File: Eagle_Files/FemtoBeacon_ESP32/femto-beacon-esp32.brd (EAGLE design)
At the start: 59.4 x 82.5 mm, 64 parts, among them IC1 FT232RQ

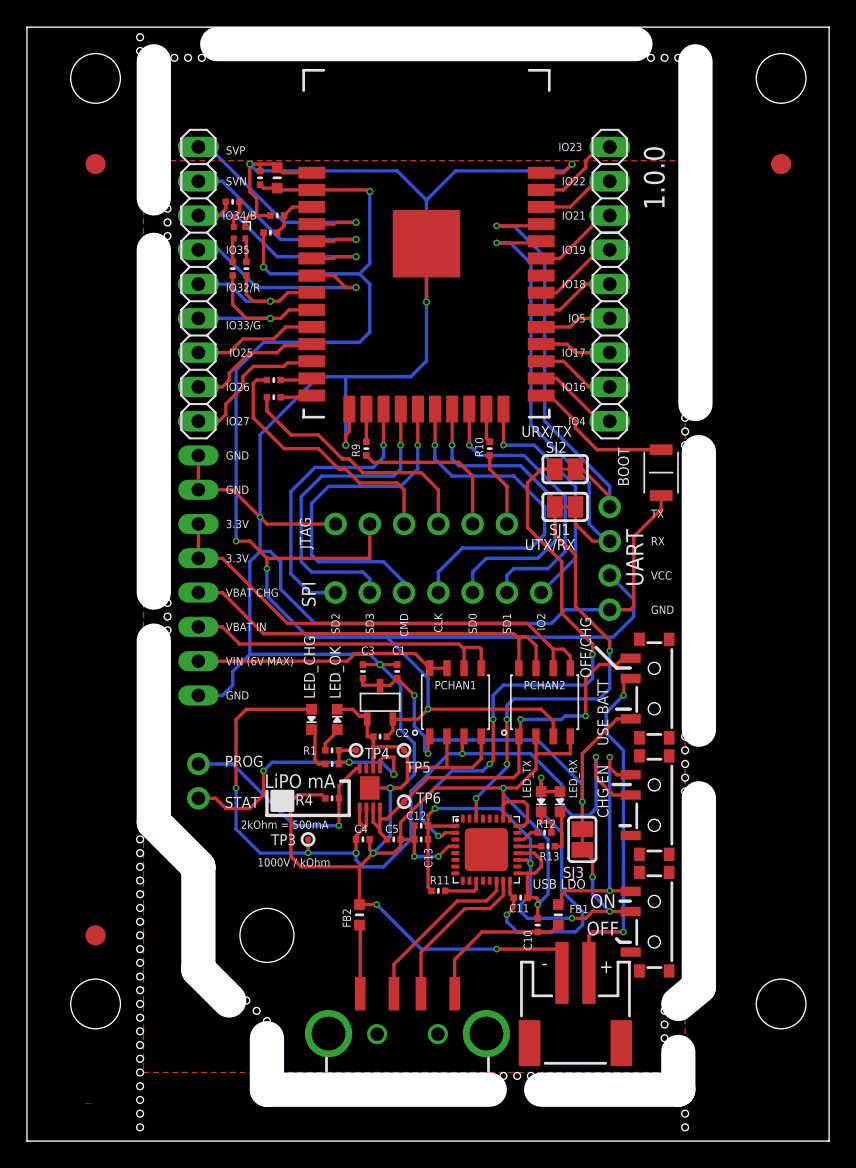
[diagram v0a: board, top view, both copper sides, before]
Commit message: Updating ESP32-WROOM-32 board. RGB Blue pin reassigned, and RGB pin 1 set to VCC instead of GND. LiPo connector pins were switched, corrected now.
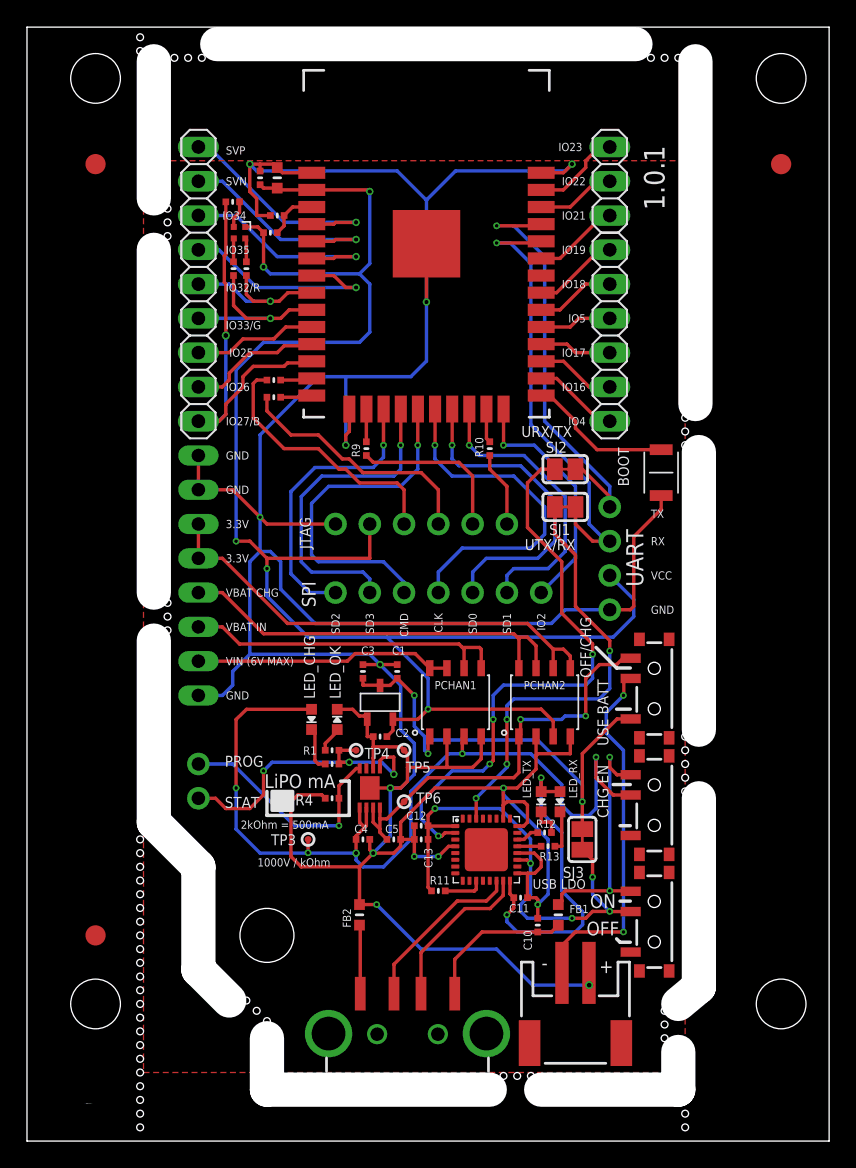
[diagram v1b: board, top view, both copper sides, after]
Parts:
- moved R15 0.06 mm to (15.3, 64.6)
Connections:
- removed net IO27: JP1.1, MOD1.12
- removed net IO34/BLUE: JP1.7, MOD1.6, R16.1
- new net IO27/BLUE: JP1.1, MOD1.12, R16.1
- new net IO34: JP1.7, MOD1.6
- net GND: now also CN_BATT_CHARGE.1; no longer CN_BATT_CHARGE.2, RGB1.1
- net VCC: now also RGB1.1
- net VLIPO: now also CN_BATT_CHARGE.2; no longer CN_BATT_CHARGE.1
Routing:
- net IO27/BLUE: track 0.00 -> 29.2 mm, vias 0 -> 1
- net IO34/BLUE: track 19.0 -> 0.00 mm, vias 1 -> 0
- net IO34: track 0.00 -> 16.3 mm, vias 0 -> 1
- net IO27: track 11.1 -> 0.00 mm
- net VLIPO: track 25.6 -> 27.2 mm
- net VCC: track 123.4 -> 124.9 mm
- net GND: track 298.9 -> 299.7 mm
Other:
- board text added: "1.0.1"
- board text added: "IO27/B"
- board text added: "IO34"
- board text removed: "1.0.0"
- board text removed: "IO27"
- board text removed: "IO34/B"
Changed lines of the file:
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@@
 <setting verticaltext="up"/>
 </settings>
-<grid distance="10" unitdist="mil" unit="mil" style="lines" multiple="1" display="no" altdistance="5" altunitdist="mil" altunit="mil"/>
+<grid distance="5" unitdist="mil" unit="mil" style="dots" multiple="1" display="yes" altdistance="5" altunitdist="mil" altunit="mil"/>
 <layers>
 <layer number="1" name="Top" color="4" fill="1" visible="yes" active="yes"/>
@@
 <text x="35.56" y="39.116" size="0.6096" layer="25" font="vector" ratio="20" rot="R270" align="center-left">SD1</text>
 <text x="38.1" y="39.116" size="0.6096" layer="25" font="vector" ratio="20" rot="R270" align="center-left">IO2</text>
-<text x="14.732" y="53.34" size="0.6096" layer="25" font="vector" ratio="20" align="center-left">IO27</text>
+<text x="14.732" y="53.34" size="0.6096" layer="25" font="vector" ratio="20" align="center-left">IO27/B</text>
 <text x="14.732" y="55.88" size="0.6096" layer="25" font="vector" ratio="20" align="center-left">IO26</text>
 <text x="14.986" y="58.42" size="0.6096" layer="25" font="vector" ratio="20" align="center-left">IO25</text>
@@
 <text x="14.732" y="63.246" size="0.6096" layer="25" font="vector" ratio="20" align="center-left">IO32/R</text>
 <text x="14.732" y="66.04" size="0.6096" layer="25" font="vector" ratio="20" align="center-left">IO35</text>
-<text x="14.478" y="68.58" size="0.6096" layer="25" font="vector" ratio="20" align="center-left">IO34/B</text>
+<text x="14.478" y="68.58" size="0.6096" layer="25" font="vector" ratio="20" align="center-left">IO34</text>
 <text x="14.732" y="71.12" size="0.6096" layer="25" font="vector" ratio="20" align="center-left">SVN</text>
 <text x="14.732" y="73.406" size="0.6096" layer="25" font="vector" ratio="20" align="center-left">SVP</text>
@@
 </polygon>
 <text x="28.194" y="43.561" size="1.524" layer="22" font="vector" ratio="20" rot="MR0" align="center">HTTPS://HACKER.HOUSE</text>
-<text x="46.482" y="71.374" size="1.524" layer="21" font="vector" ratio="20" rot="R90" align="center">1.0.0</text>
+<text x="46.482" y="71.374" size="1.524" layer="21" font="vector" ratio="20" rot="R90" align="center">1.0.1</text>
 <text x="42.672" y="17.78" size="1.016" layer="21" font="vector" ratio="20" rot="R180" align="center">ON</text>
 <text x="42.672" y="15.748" size="1.016" layer="21" font="vector" ratio="20" rot="R180" align="center">OFF</text>
@@
 <attribute name="MPN" value="CRCW0402270RFKED" x="16.256" y="64.643" size="1.778" layer="27" rot="R90" display="off"/>
 </element>
-<element name="R15" library="microbuilder" package="_0402MP" value="270" x="15.24" y="64.643" smashed="yes" rot="R90">
-<attribute name="MPN" value="CRCW0402270RFKED" x="15.24" y="64.643" size="1.778" layer="27" rot="R90" display="off"/>
+<element name="R15" library="microbuilder" package="_0402MP" value="270" x="15.3035" y="64.643" smashed="yes" rot="R90">
+<attribute name="MPN" value="CRCW0402270RFKED" x="15.3035" y="64.643" size="1.778" layer="27" rot="R90" display="off"/>
 </element>
 <element name="R16" library="microbuilder" package="_0402MP" value="270" x="15.24" y="69.596" smashed="yes">
@@
 <wire x1="44.958" y1="38.862" x2="43.434" y2="37.338" width="0.254" layer="16"/>
 <wire x1="43.434" y1="37.338" x2="26.67" y2="37.338" width="0.254" layer="16"/>
+<contactref element="RGB1" pad="1"/>
+<wire x1="16.173" y1="67.735" x2="17.101" y2="67.735" width="0.254" layer="1"/>
+<wire x1="17.101" y1="67.735" x2="17.526" y2="67.31" width="0.254" layer="1"/>
 </signal>
 <signal name="GND">
@@
 <contactref element="BOOT" pad="2"/>
 <contactref element="UART" pad="1"/>
-<contactref element="CN_BATT_CHARGE" pad="2"/>
 <contactref element="FB2" pad="2"/>
 <contactref element="IC1" pad="24"/>
@@
 <contactref element="C12" pad="1"/>
 <contactref element="C13" pad="1"/>
-<contactref element="RGB1" pad="1"/>
 <wire x1="18.542" y1="72.136" x2="18.928" y2="71.75" width="0.254" layer="1"/>
 <wire x1="18.542" y1="72.136" x2="18.288" y2="72.39" width="0.254" layer="1"/>
-<wire x1="16.173" y1="67.735" x2="16.173" y2="68.243" width="0.254" layer="1"/>
-<wire x1="16.173" y1="68.243" x2="16.51" y2="68.58" width="0.254" layer="1"/>
-<wire x1="16.51" y1="68.58" x2="17.018" y2="68.58" width="0.254" layer="1"/>
 <wire x1="17.018" y1="68.58" x2="18.034" y2="68.58" width="0.254" layer="1"/>
 <wire x1="17.272" y1="72.39" x2="16.51" y2="72.39" width="0.254" layer="1"/>
@@
 <wire x1="39.878" y1="39.37" x2="38.862" y2="38.354" width="0.254" layer="16"/>
 <wire x1="38.862" y1="38.354" x2="21.336" y2="38.354" width="0.254" layer="16"/>
-<wire x1="39.64" y1="12.463" x2="39.64" y2="14.208" width="0.254" layer="1"/>
-<wire x1="39.64" y1="14.208" x2="39.624" y2="14.224" width="0.254" layer="1"/>
-<wire x1="39.624" y1="14.224" x2="34.798" y2="14.224" width="0.254" layer="1"/>
-<via x="34.798" y="14.224" extent="1-16" drill="0.254" diameter="0.508"/>
 <wire x1="34.798" y1="14.224" x2="29.21" y2="14.224" width="0.254" layer="16"/>
 <wire x1="29.21" y1="14.224" x2="25.908" y2="17.526" width="0.254" layer="16"/>
@@
 <wire x1="21.336" y1="38.354" x2="18.796" y2="40.894" width="0.254" layer="16"/>
 <wire x1="18.796" y1="40.894" x2="18.796" y2="42.926" width="0.254" layer="16"/>
+<contactref element="CN_BATT_CHARGE" pad="1"/>
+<wire x1="41.64" y1="12.463" x2="41.656" y2="12.447" width="0.254" layer="1"/>
+<wire x1="41.656" y1="12.447" x2="41.656" y2="11.557" width="0.254" layer="1"/>
+<via x="41.656" y="11.557" extent="1-16" drill="0.35"/>
+<wire x1="41.656" y1="11.557" x2="37.465" y2="11.557" width="0.254" layer="16"/>
+<wire x1="37.465" y1="11.557" x2="34.798" y2="14.224" width="0.254" layer="16"/>
 </signal>
 <signal name="SD1">
@@
 <wire x1="14.478" y1="71.12" x2="12.7" y2="71.12" width="0.254" layer="16"/>
 </signal>
-<signal name="IO34/BLUE">
+<signal name="IO34">
 <contactref element="MOD1" pad="6"/>
 <contactref element="JP1" pad="7"/>
-<contactref element="R16" pad="1"/>
-<wire x1="14.224" y1="68.58" x2="12.7" y2="68.58" width="0.254" layer="1"/>
 <wire x1="24.384" y1="65.532" x2="22.86" y2="65.532" width="0.254" layer="1"/>
 <wire x1="22.86" y1="65.532" x2="22.728" y2="65.4" width="0.254" layer="1"/>
@@
 <wire x1="15.494" y1="68.58" x2="12.7" y2="68.58" width="0.254" layer="16"/>
 <wire x1="18.542" y1="65.532" x2="15.494" y2="68.58" width="0.254" layer="16"/>
-<wire x1="14.732" y1="69.596" x2="14.732" y2="69.088" width="0.254" layer="1"/>
-<wire x1="14.732" y1="69.088" x2="14.224" y2="68.58" width="0.254" layer="1"/>
 </signal>
 <signal name="IO35">
@@
 <wire x1="18.796" y1="60.96" x2="18.034" y2="60.96" width="0.254" layer="1"/>
 <wire x1="18.034" y1="60.96" x2="16.256" y2="60.96" width="0.254" layer="1"/>
-<wire x1="16.256" y1="60.96" x2="15.24" y2="61.976" width="0.254" layer="1"/>
-<wire x1="15.24" y1="61.976" x2="15.24" y2="64.135" width="0.254" layer="1"/>
+<wire x1="16.256" y1="60.96" x2="15.3035" y2="61.9125" width="0.254" layer="1"/>
+<wire x1="15.3035" y1="61.9125" x2="15.3035" y2="64.135" width="0.254" layer="1"/>
 </signal>
 <signal name="IO25">
@@
 <wire x1="20.978" y1="58.928" x2="19.05" y2="58.928" width="0.254" layer="1"/>
 </signal>
-<signal name="IO27">
+<signal name="IO27/BLUE">
 <contactref element="MOD1" pad="12"/>
 <contactref element="JP1" pad="1"/>
@@
 <wire x1="20.978" y1="57.658" x2="19.304" y2="57.658" width="0.254" layer="1"/>
 <wire x1="16.002" y1="56.642" x2="16.002" y2="55.88" width="0.254" layer="1"/>
+<contactref element="R16" pad="1"/>
+<wire x1="14.732" y1="69.596" x2="14.732" y2="65.69053125" width="0.254" layer="1"/>
+<wire x1="14.732" y1="65.69053125" x2="14.6217" y2="65.58023125" width="0.254" layer="1"/>
+<wire x1="14.6217" y1="63.61686875" x2="14.732" y2="63.50656875" width="0.254" layer="1"/>
+<wire x1="14.6217" y1="65.58023125" x2="14.6217" y2="63.61686875" width="0.254" layer="1"/>
+<via x="14.732" y="59.69" extent="1-16" drill="0.35"/>
+<wire x1="14.732" y1="59.69" x2="14.732" y2="53.848" width="0.254" layer="16"/>
+<wire x1="14.224" y1="53.34" x2="12.7" y2="53.34" width="0.254" layer="16"/>
+<wire x1="14.732" y1="63.50656875" x2="14.732" y2="59.69" width="0.254" layer="1"/>
+<wire x1="14.732" y1="53.848" x2="14.224" y2="53.34" width="0.254" layer="16"/>
 </signal>
 <signal name="IO2">
@@
 </signal>
 <signal name="VLIPO">
-<contactref element="CN_BATT_CHARGE" pad="1"/>
 <contactref element="SW_BATTMODE" pad="B"/>
-<wire x1="41.64" y1="12.463" x2="41.64" y2="15.224" width="0.254" layer="1"/>
-<wire x1="41.91" y1="15.494" x2="44.196" y2="15.494" width="0.254" layer="1"/>
-<wire x1="41.91" y1="15.494" x2="41.64" y2="15.224" width="0.254" layer="1"/>
 <via x="44.196" y="15.494" extent="1-16" drill="0.254" diameter="0.508"/>
 <wire x1="44.196" y1="28.956" x2="44.196" y2="15.494" width="0.254" layer="16"/>
@@
 <wire x1="44.224" y1="34.024" x2="44.224" y2="33.048" width="0.254" layer="1"/>
 <wire x1="44.196" y1="28.956" x2="42.926" y2="30.226" width="0.254" layer="16"/>
+<contactref element="CN_BATT_CHARGE" pad="2"/>
+<wire x1="39.64" y1="12.463" x2="39.64" y2="14.494" width="0.254" layer="1"/>
+<wire x1="39.64" y1="14.494" x2="40.64" y2="15.494" width="0.254" layer="1"/>
+<wire x1="40.64" y1="15.494" x2="44.196" y2="15.494" width="0.254" layer="1"/>
 </signal>
 <signal name="VIN_LDO">
@@
 <contactref element="RGB1" pad="3"/>
 <contactref element="R15" pad="2"/>
-<wire x1="15.323" y1="66.885" x2="15.24" y2="66.802" width="0.254" layer="1"/>
-<wire x1="15.24" y1="66.802" x2="15.24" y2="65.151" width="0.254" layer="1"/>
+<wire x1="15.323" y1="66.885" x2="15.3035" y2="66.8655" width="0.254" layer="1"/>
+<wire x1="15.3035" y1="66.8655" x2="15.3035" y2="65.151" width="0.254" layer="1"/>
 </signal>
 <signal name="N$11">
